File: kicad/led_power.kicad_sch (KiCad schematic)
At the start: 3 parts

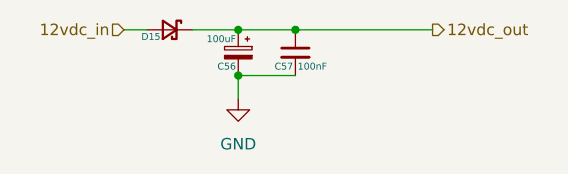
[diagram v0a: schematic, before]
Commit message: Update SCCS-RPI KiCad design and production files
Add GPS RF ESD and matching (ESD103-B1-02EL, 27nH, 10R, 100nF),
swap the 10A fuses to A16-1000, retune copper zone fills, and
regenerate BOM, positions, netlist, gerbers, and schematics PDF.
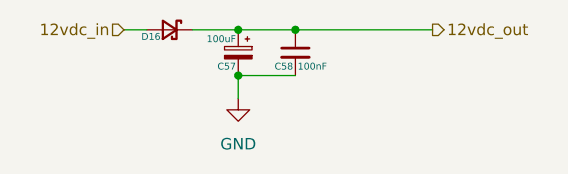
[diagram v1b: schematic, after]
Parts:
- renumbered C56 to C57, C57 to C58, D15 to D16
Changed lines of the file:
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@@
 		(in_pos_files yes)
 		(dnp no)
-		(property "Reference" "C56"
+		(property "Reference" "C57"
 			(at 96.266 65.024 0)
 			(show_name no)
@@
 			(project "SCCS-RPI"
 				(path "/ce21946f-7655-4864-b48a-50deff8538eb/289c7879-c293-41e1-9b12-36ce1916fe2d"
-					(reference "C56")
+					(reference "C57")
 					(unit 1)
 				)
 				(path "/ce21946f-7655-4864-b48a-50deff8538eb/a0eedc41-812c-454a-9c61-ce155b766160"
-					(reference "C58")
+					(reference "C59")
 					(unit 1)
 				)
 				(path "/ce21946f-7655-4864-b48a-50deff8538eb/a3c5f999-1a2d-4d52-a7d9-976e13506cfb"
-					(reference "C60")
+					(reference "C61")
 					(unit 1)
 				)
 				(path "/ce21946f-7655-4864-b48a-50deff8538eb/f9fe6a99-0547-4304-8cea-93a9433511c0"
-					(reference "C62")
+					(reference "C63")
 					(unit 1)
 				)
@@
 		(in_pos_files yes)
 		(dnp no)
-		(property "Reference" "D15"
+		(property "Reference" "D16"
 			(at 87.884 61.722 0)
 			(show_name no)
@@
 			(project "SCCS-RPI"
 				(path "/ce21946f-7655-4864-b48a-50deff8538eb/289c7879-c293-41e1-9b12-36ce1916fe2d"
-					(reference "D15")
+					(reference "D16")
 					(unit 1)
 				)
 				(path "/ce21946f-7655-4864-b48a-50deff8538eb/a0eedc41-812c-454a-9c61-ce155b766160"
-					(reference "D16")
+					(reference "D17")
 					(unit 1)
 				)
 				(path "/ce21946f-7655-4864-b48a-50deff8538eb/a3c5f999-1a2d-4d52-a7d9-976e13506cfb"
-					(reference "D17")
+					(reference "D18")
 					(unit 1)
 				)
 				(path "/ce21946f-7655-4864-b48a-50deff8538eb/f9fe6a99-0547-4304-8cea-93a9433511c0"
-					(reference "D18")
+					(reference "D19")
 					(unit 1)
 				)
@@
 		(in_pos_files yes)
 		(dnp no)
-		(property "Reference" "C57"
+		(property "Reference" "C58"
 			(at 102.616 65.024 0)
 			(show_name no)
@@
 			(project "SCCS-RPI"
 				(path "/ce21946f-7655-4864-b48a-50deff8538eb/289c7879-c293-41e1-9b12-36ce1916fe2d"
-					(reference "C57")
+					(reference "C58")
 					(unit 1)
 				)
 				(path "/ce21946f-7655-4864-b48a-50deff8538eb/a0eedc41-812c-454a-9c61-ce155b766160"
-					(reference "C59")
+					(reference "C60")
 					(unit 1)
 				)
 				(path "/ce21946f-7655-4864-b48a-50deff8538eb/a3c5f999-1a2d-4d52-a7d9-976e13506cfb"
-					(reference "C61")
+					(reference "C62")
 					(unit 1)
 				)
 				(path "/ce21946f-7655-4864-b48a-50deff8538eb/f9fe6a99-0547-4304-8cea-93a9433511c0"
-					(reference "C63")
-					(unit 1)
-				)
+					(reference "C64")
+					(unit 1)
+				)

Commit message: Update SCCS-RPI KiCad design and production files
Split 5V and 3V3 regulation onto dedicated Power sheets with a second
AP64501 buck, extra inductor and passives, update the enclosure
bracket, and regenerate BOM, positions, netlist, gerbers, and
schematics PDF.
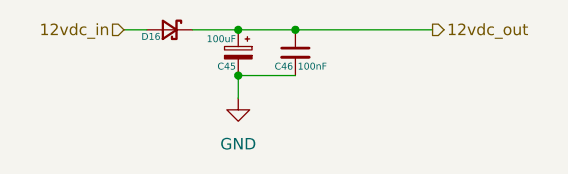
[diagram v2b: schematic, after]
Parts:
- renumbered C57 to C45, C58 to C46
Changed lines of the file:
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@@
 		(in_pos_files yes)
 		(dnp no)
-		(property "Reference" "C57"
+		(property "Reference" "C45"
 			(at 96.266 65.024 0)
 			(show_name no)
@@
 			(project "SCCS-RPI"
 				(path "/ce21946f-7655-4864-b48a-50deff8538eb/289c7879-c293-41e1-9b12-36ce1916fe2d"
-					(reference "C57")
+					(reference "C45")
 					(unit 1)
 				)
 				(path "/ce21946f-7655-4864-b48a-50deff8538eb/a0eedc41-812c-454a-9c61-ce155b766160"
-					(reference "C59")
+					(reference "C47")
 					(unit 1)
 				)
 				(path "/ce21946f-7655-4864-b48a-50deff8538eb/a3c5f999-1a2d-4d52-a7d9-976e13506cfb"
-					(reference "C61")
+					(reference "C49")
 					(unit 1)
 				)
 				(path "/ce21946f-7655-4864-b48a-50deff8538eb/f9fe6a99-0547-4304-8cea-93a9433511c0"
-					(reference "C63")
+					(reference "C51")
 					(unit 1)
 				)
@@
 		(dnp no)
 		(fields_autoplaced yes)
-		(property "Reference" "#PWR073"
+		(property "Reference" "#PWR072"
 			(at 96.52 74.93 0)
 			(hide yes)
@@
 			(project "SCCS-RPI"
 				(path "/ce21946f-7655-4864-b48a-50deff8538eb/289c7879-c293-41e1-9b12-36ce1916fe2d"
+					(reference "#PWR072")
+					(unit 1)
+				)
+				(path "/ce21946f-7655-4864-b48a-50deff8538eb/a0eedc41-812c-454a-9c61-ce155b766160"
 					(reference "#PWR073")
 					(unit 1)
 				)
-				(path "/ce21946f-7655-4864-b48a-50deff8538eb/a0eedc41-812c-454a-9c61-ce155b766160"
+				(path "/ce21946f-7655-4864-b48a-50deff8538eb/a3c5f999-1a2d-4d52-a7d9-976e13506cfb"
 					(reference "#PWR074")
 					(unit 1)
 				)
-				(path "/ce21946f-7655-4864-b48a-50deff8538eb/a3c5f999-1a2d-4d52-a7d9-976e13506cfb"
+				(path "/ce21946f-7655-4864-b48a-50deff8538eb/f9fe6a99-0547-4304-8cea-93a9433511c0"
 					(reference "#PWR075")
-					(unit 1)
-				)
-				(path "/ce21946f-7655-4864-b48a-50deff8538eb/f9fe6a99-0547-4304-8cea-93a9433511c0"
-					(reference "#PWR076")
 					(unit 1)
 				)
@@
 		(in_pos_files yes)
 		(dnp no)
-		(property "Reference" "C58"
+		(property "Reference" "C46"
 			(at 102.616 65.024 0)
 			(show_name no)
@@
 			(project "SCCS-RPI"
 				(path "/ce21946f-7655-4864-b48a-50deff8538eb/289c7879-c293-41e1-9b12-36ce1916fe2d"
-					(reference "C58")
+					(reference "C46")
 					(unit 1)
 				)
 				(path "/ce21946f-7655-4864-b48a-50deff8538eb/a0eedc41-812c-454a-9c61-ce155b766160"
-					(reference "C60")
+					(reference "C48")
 					(unit 1)
 				)
 				(path "/ce21946f-7655-4864-b48a-50deff8538eb/a3c5f999-1a2d-4d52-a7d9-976e13506cfb"
-					(reference "C62")
+					(reference "C50")
 					(unit 1)
 				)
 				(path "/ce21946f-7655-4864-b48a-50deff8538eb/f9fe6a99-0547-4304-8cea-93a9433511c0"
-					(reference "C64")
-					(unit 1)
-				)
+					(reference "C52")
+					(unit 1)
+				)
